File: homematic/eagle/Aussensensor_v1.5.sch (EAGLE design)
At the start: 45 parts, among them IC1 Atmega 328P, IC2 MAX1724, IC3 MAX44009, IC4 TSL256FN, IC5 BMP180, IC6 BME280, IC7 DS18B20, M1 CC1101_WIRELES_MODULE, T1 IRML6344

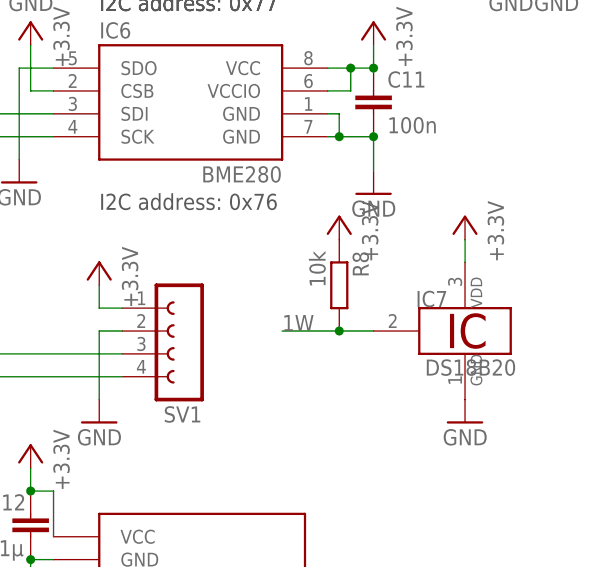
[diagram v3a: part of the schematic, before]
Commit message: update to previous version: - changed pull-up to 4k7 in Aussensensor_v1.5.sch and brd - added Aussensensor_v1.5_bom.xls
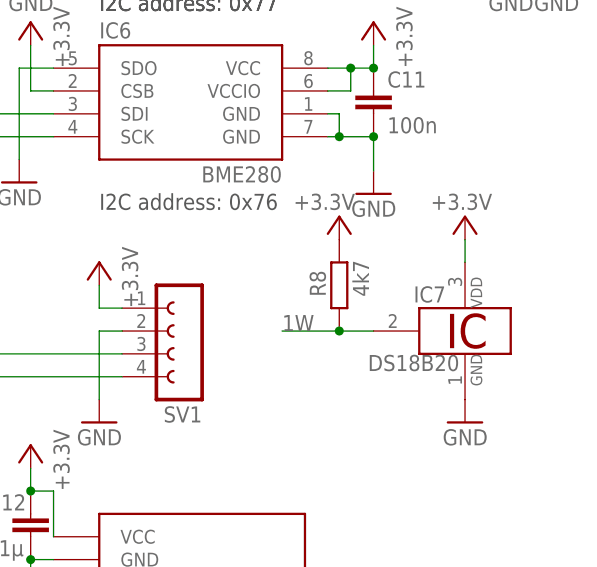
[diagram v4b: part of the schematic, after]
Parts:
- R8: value 10k -> 4k7
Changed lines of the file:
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@@
 <part name="P+11" library="supply1" deviceset="+5V" device="" value="+3.3V"/>
 <part name="GND21" library="supply1" deviceset="GND" device=""/>
-<part name="R8" library="rcl" deviceset="R-EU_" device="M0805" value="10k"/>
+<part name="R8" library="rcl" deviceset="R-EU_" device="M0805" value="4k7"/>
 <part name="P+12" library="supply1" deviceset="+5V" device="" value="+3.3V"/>
 <part name="C12" library="rcl" deviceset="C-EU" device="C0805" value="1µ"/>
@@
 <instance part="C11" gate="G$1" x="238.76" y="118.11"/>
 <instance part="IC7" gate="A" x="248.92" y="91.44" smashed="yes" rot="R180">
-<attribute name="NAME" x="247.015" y="95.885" size="1.778" layer="95" rot="R180"/>
-<attribute name="VALUE" x="254.635" y="88.265" size="1.778" layer="96" rot="R180"/>
+<attribute name="NAME" x="243.205" y="94.615" size="1.778" layer="95"/>
+<attribute name="VALUE" x="238.125" y="86.995" size="1.778" layer="96"/>
 </instance>
 <instance part="IC7" gate="P" x="248.92" y="91.44" smashed="yes"/>
 <instance part="IC7" gate="_1W" x="243.84" y="91.44" smashed="yes"/>
-<instance part="P+11" gate="1" x="248.92" y="104.14" rot="MR0"/>
+<instance part="P+11" gate="1" x="248.92" y="104.14" smashed="yes" rot="MR0">
+<attribute name="VALUE" x="245.11" y="106.68" size="1.778" layer="96" rot="MR180"/>
+</instance>
 <instance part="GND21" gate="1" x="248.92" y="81.28" rot="MR0"/>
-<instance part="R8" gate="G$1" x="234.95" y="96.52" rot="R270"/>
-<instance part="P+12" gate="1" x="234.95" y="104.14" rot="MR0"/>
+<instance part="R8" gate="G$1" x="234.95" y="96.52" smashed="yes" rot="R270">
+<attribute name="NAME" x="233.4514" y="95.25" size="1.778" layer="95" rot="R90"/>
+<attribute name="VALUE" x="238.252" y="95.25" size="1.778" layer="96" rot="R90"/>
+</instance>
+<instance part="P+12" gate="1" x="234.95" y="104.14" smashed="yes" rot="MR0">
+<attribute name="VALUE" x="229.87" y="106.68" size="1.778" layer="96" rot="MR180"/>
+</instance>
 <instance part="C12" gate="G$1" x="200.66" y="71.12" smashed="yes">
 <attribute name="NAME" x="195.834" y="71.501" size="1.778" layer="95"/>

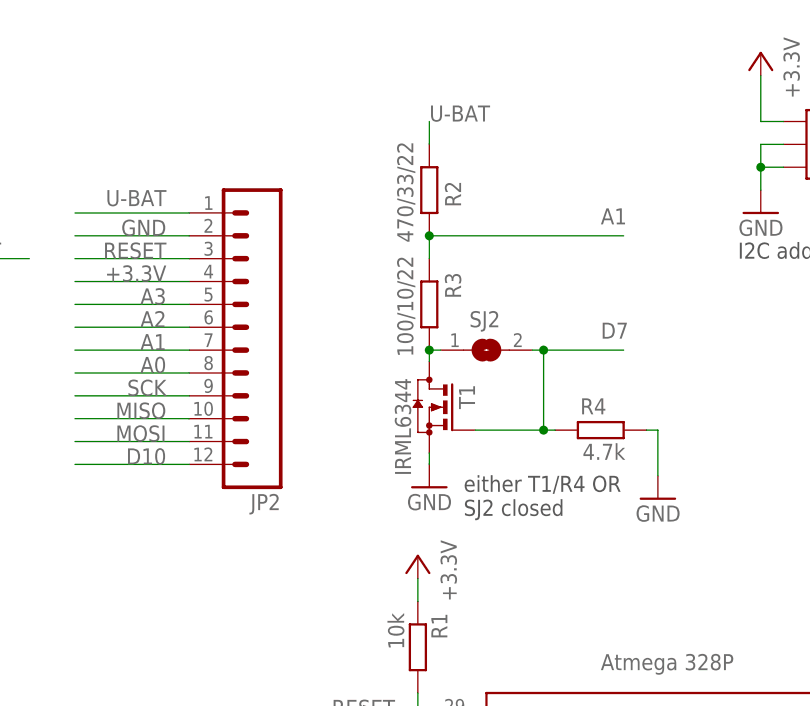
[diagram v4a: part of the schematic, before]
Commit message: Changes to previous version: - updated R-divider for voltage measurement in Aussensensor_v1.5_bom.xls and the eagle files, printed PDF of schematic (Aussensensor_v1.5_sch.pdf)
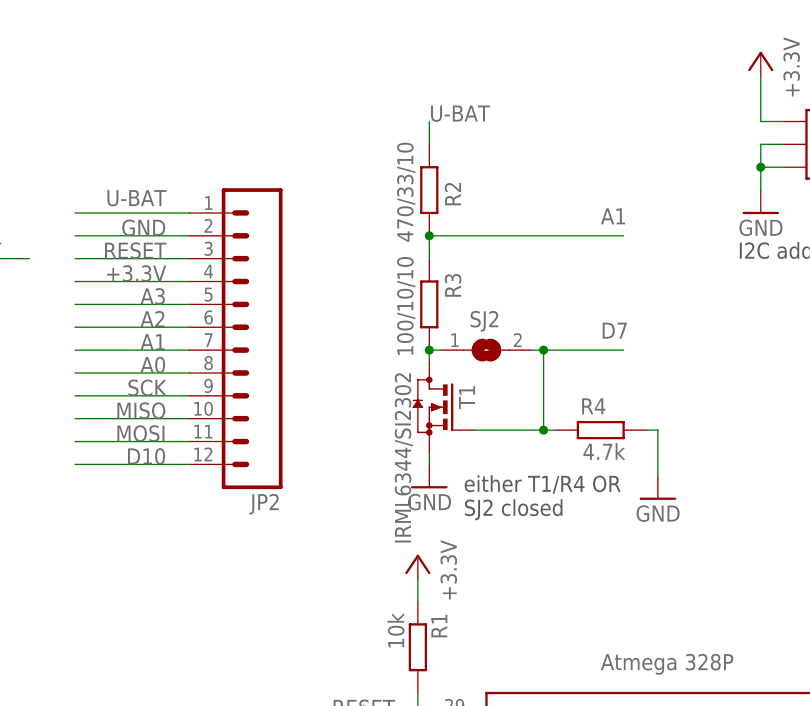
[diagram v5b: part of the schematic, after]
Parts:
- R2: value 470/33/22 -> 470/33/10
- R3: value 100/10/22 -> 100/10/10
- T1: value IRML6344 -> IRML6344/SI2302
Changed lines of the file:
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@@
 <setting verticaltext="up"/>
 </settings>
-<grid distance="50" unitdist="mil" unit="mil" style="lines" multiple="1" display="no" altdistance="0.01" altunitdist="inch" altunit="inch"/>
+<grid distance="0.1" unitdist="inch" unit="inch" style="lines" multiple="1" display="no" altdistance="0.01" altunitdist="inch" altunit="inch"/>
 <layers>
 <layer number="1" name="Top" color="4" fill="1" visible="no" active="no"/>
@@
 <part name="SJ1" library="jumper" deviceset="SJ" device=""/>
 <part name="CONFIG" library="switch-tact" deviceset="DTSM-3" device=""/>
-<part name="R2" library="rcl" deviceset="R-EU_" device="M0805" value="470/33/22"/>
-<part name="R3" library="rcl" deviceset="R-EU_" device="M0805" value="100/10/22"/>
+<part name="R2" library="rcl" deviceset="R-EU_" device="M0805" value="470/33/10"/>
+<part name="R3" library="rcl" deviceset="R-EU_" device="M0805" value="100/10/10"/>
 <part name="FRAME1" library="frames" deviceset="DINA4_L" device=""/>
 <part name="PAD1" library="wirepad" deviceset="SMD2" device=""/>
@@
 <part name="C12" library="rcl" deviceset="C-EU" device="C0805" value="1µ"/>
 <part name="C10" library="rcl" deviceset="CPOL-EU" device="SMCA" value="22µ"/>
-<part name="T1" library="transistor-small-signal" deviceset="BSS123" device="" value="IRML6344"/>
+<part name="T1" library="transistor-small-signal" deviceset="BSS123" device="" value="IRML6344/SI2302"/>
 <part name="R4" library="rcl" deviceset="R-EU_" device="M0805" value="4.7k"/>
 <part name="GND20" library="supply1" deviceset="GND" device=""/>
@@
 <instance part="T1" gate="G$1" x="90.17" y="135.89" smashed="yes" rot="MR0">
 <attribute name="NAME" x="95.25" y="138.43" size="1.778" layer="95" rot="MR270"/>
-<attribute name="VALUE" x="86.36" y="128.27" size="1.778" layer="96" rot="MR90"/>
+<attribute name="VALUE" x="86.36" y="120.65" size="1.778" layer="96" rot="MR90"/>
 </instance>
 <instance part="R4" gate="G$1" x="109.22" y="133.35" smashed="yes">
